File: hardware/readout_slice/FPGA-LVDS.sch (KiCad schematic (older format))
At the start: 8 parts

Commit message: auto push run at Wed Apr 14 11:00:44 EDT 2021
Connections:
- wire segments 40 -> 44
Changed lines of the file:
@@
 Text HLabel 1650 3250 0    50   Input ~ 0
 Raz_Chn_p
-Text HLabel 1650 3450 0    50   Input ~ 0
+Text HLabel 1650 3350 0    50   Input ~ 0
 Raz_chn_n
 Text HLabel 1650 3550 0    50   Input ~ 0
 Val_Ext_p
-Text HLabel 1650 3750 0    50   Input ~ 0
+Text HLabel 1650 3650 0    50   Input ~ 0
 Val_Ext_n
+Wire Wire Line
+	1650 3250 1800 3250
+Wire Wire Line
+	1650 3350 1800 3350
+Wire Wire Line
+	1650 3550 1800 3550
+Wire Wire Line
+	1650 3650 1800 3650
 $EndSCHEMATC

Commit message: auto push run at Tue Apr 20 18:13:16 EDT 2021
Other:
- note added: "always point to point\n2 chips -> 2 sets of signals"
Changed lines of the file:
@@
 Wire Wire Line
 	1650 3650 1800 3650
+Text Notes 750  3550 0    50   ~ 0
+always point to point\n2 chips -> 2 sets of signals
 $EndSCHEMATC

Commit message: auto push run at Wed Apr 21 10:59:57 EDT 2021
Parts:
- added C?: 0.01u, symbol Device:C_Small
- added J?: jumper, symbol Connector_Generic:Conn_01x03
- added R?: 100, symbol Device:R_Small
- added U?: XLXO, symbol readout:XLXO
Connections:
- net labels added: +3V3, ADC_CS_1, ADC_CS_2, ADC_SCLK_1, ADC_SCLK_2, ADC_SDI_1, ADC_SDI_2, ADC_SDO_1, ADC_SDO_2, LVDS_GPIO_n1, LVDS_GPIO_n2, LVDS_GPIO_p1, LVDS_GPIO_p2, Raz_Chn_p1, Raz_Chn_p2, Raz_chn_n1, Raz_chn_n2, Val_Ext_n1, Val_Ext_n2, Val_Ext_p1, Val_Ext_p2
- net labels removed: Raz_Chn_p, Raz_chn_n, Val_Ext_n, Val_Ext_p
- wire segments 44 -> 78
- no-connect marks 0 -> 1
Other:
- note added: "double check footprints,\nosc datasheets can be strange"
- note added: "replace\n"
- note removed: "always point to point\n2 chips -> 2 sets of signals"
- moved on the sheet: U?E

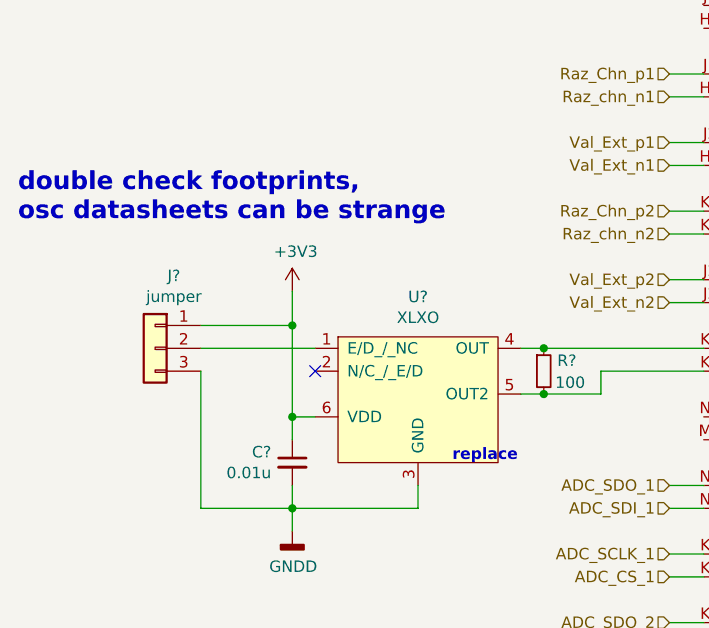
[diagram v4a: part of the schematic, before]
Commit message: removed zx2, added sfp for serdes from dan's vice board
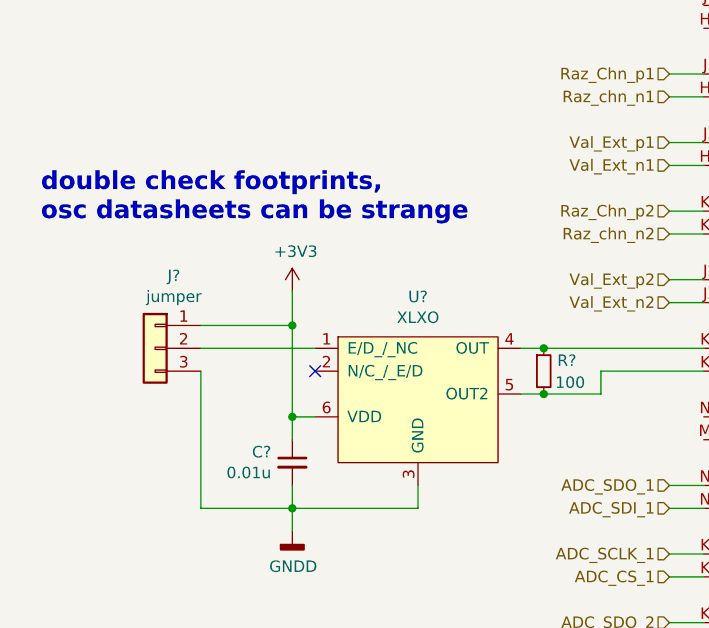
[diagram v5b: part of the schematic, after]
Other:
- note removed: "replace\n"
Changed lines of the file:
@@
 $Descr A4 11693 8268
 encoding utf-8
-Sheet 5 14
+Sheet 3 11
 Title ""
 Date ""
@@
 Wire Wire Line
 	1500 4450 1000 4450
-Text Notes 2100 4950 0    50   ~ 10
-replace\n
 NoConn ~ 1500 4550
 Text HLabel 3050 5050 0    50   Input ~ 0
@@
 Text HLabel 3050 5950 0    50   Input ~ 0
 ADC_SCLK_2
-Text Notes 200  3900 0    79   ~ 16
+Text Notes 300  3900 0    79   ~ 16
 double check footprints,\nosc datasheets can be strange
 $Comp

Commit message: auto push run at Wed Apr 28 10:36:58 EDT 2021
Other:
- moved on the sheet: C?, J?, R?, U?, U?E

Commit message: working on power
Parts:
- added U? (x2): Vcc0_2v5, symbol readout:VccSFP
- added U?: Vcc0_3v3, symbol readout:Vcc0
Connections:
- net +3V3 is gone; now on net VCC: C?.1, J?.1 (Pin_1), U?.6 (VDD)
- net +2V5 renamed VCC
- net VCC: now also U?.1 (VCC), U?.1 (VCC), U?.1 (VCC)
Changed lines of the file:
@@
 Text Notes 3450 1700 0    157  ~ 31
 LVDS Bank
-$Comp
-L power:+2V5 #PWR?
-U 1 1 607849FE
-P 11000 700
-F 0 "#PWR?" H 11000 550 50  0001 C CNN
-F 1 "+2V5" H 11000 850 50  0000 C CNB
-F 2 "" H 11000 700 50  0001 C CNN
-F 3 "" H 11000 700 50  0001 C CNN
-	1    11000 700
-	1    0    0    -1
-$EndComp
 Wire Wire Line
 	11000 800  11000 750
@@
 	11000 1150 11000 1050
 Connection ~ 11000 1050
-$Comp
-L power:+2V5 #PWR?
-U 1 1 6079C1E3
-P 6900 1750
-F 0 "#PWR?" H 6900 1600 50  0001 C CNN
-F 1 "+2V5" H 6900 1900 50  0000 C CNB
-F 2 "" H 6900 1750 50  0001 C CNN
-F 3 "" H 6900 1750 50  0001 C CNN
-	1    6900 1750
-	1    0    0    -1
-$EndComp
 Wire Wire Line
 	6900 1950 6900 1900
@@
 Connection ~ 3450 4200
 $Comp
-L power:+3V3 #PWR?
-U 1 1 6091AF5E
-P 3450 3650
-F 0 "#PWR?" H 3450 3500 50  0001 C CNN
-F 1 "+3V3" H 3465 3823 50  0000 C CNN
-F 2 "" H 3450 3650 50  0001 C CNN
-F 3 "" H 3450 3650 50  0001 C CNN
-	1    3450 3650
-	1    0    0    -1
-$EndComp
-$Comp
 L Device:R_Small R?
 U 1 1 609246AE
@@
 Wire Wire Line
 	3450 3800 3450 3650
+$Comp
+L readout:VccSFP U?
+U 1 1 60AB36FC
+P 6900 1650
+AR Path="/62251D77/60AB36FC" Ref="U?"  Part="1"
+AR Path="/60768143/60AB36FC" Ref="U?"  Part="1"
+F 0 "U?" H 6900 1650 79  0001 C CNN
+F 1 "Vcc0_2v5" H 6750 1700 47  0000 L CNB
+F 2 "" H 6900 1650 79  0001 C CNN
+F 3 "" H 6900 1650 79  0001 C CNN
+	1    6900 1650
+	1    0    0    -1
+$EndComp
+$Comp
+L readout:VccSFP U?
+U 1 1 60AB9DC8
+P 11000 600
+AR Path="/62251D77/60AB9DC8" Ref="U?"  Part="1"
+AR Path="/60768143/60AB9DC8" Ref="U?"  Part="1"
+F 0 "U?" H 11000 600 79  0001 C CNN
+F 1 "Vcc0_2v5" H 10850 650 47  0000 L CNB
+F 2 "" H 11000 600 79  0001 C CNN
+F 3 "" H 11000 600 79  0001 C CNN
+	1    11000 600
+	1    0    0    -1
+$EndComp
+$Comp
+L readout:Vcc0 U?
+U 1 1 60D73E04
+P 3450 3550
+AR Path="/6076C700/60D73E04" Ref="U?"  Part="1"
+AR Path="/62251D77/60D73E04" Ref="U?"  Part="1"
+AR Path="/608CAA95/60D73E04" Ref="U?"  Part="1"
+AR Path="/60768143/60D73E04" Ref="U?"  Part="1"
+F 0 "U?" H 3450 3550 79  0001 C CNN
+F 1 "Vcc0_3v3" H 3300 3600 47  0000 L CNB
+F 2 "" H 3450 3550 79  0001 C CNN
+F 3 "" H 3450 3550 79  0001 C CNN
+	1    3450 3550
+	1    0    0    -1
+$EndComp
 $EndSCHEMATC
